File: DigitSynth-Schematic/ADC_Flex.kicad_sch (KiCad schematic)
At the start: 3 parts, among them U1 ADS1256IDBR

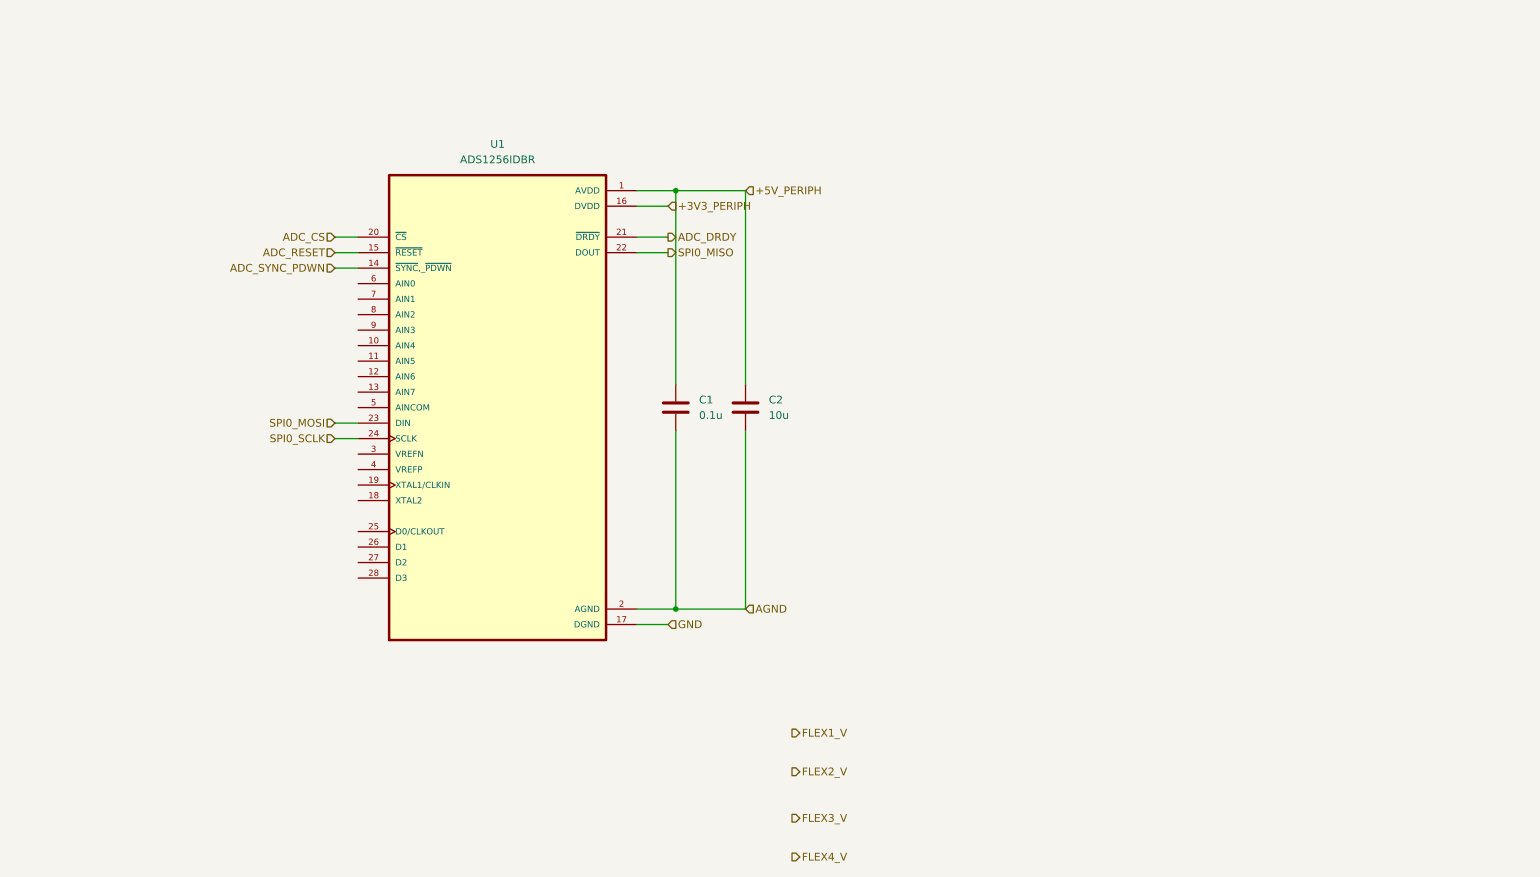
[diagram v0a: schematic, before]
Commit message: Add completed KiCad schematic hierarchy (Pi interface, ADC, LEDs, buttons, power)
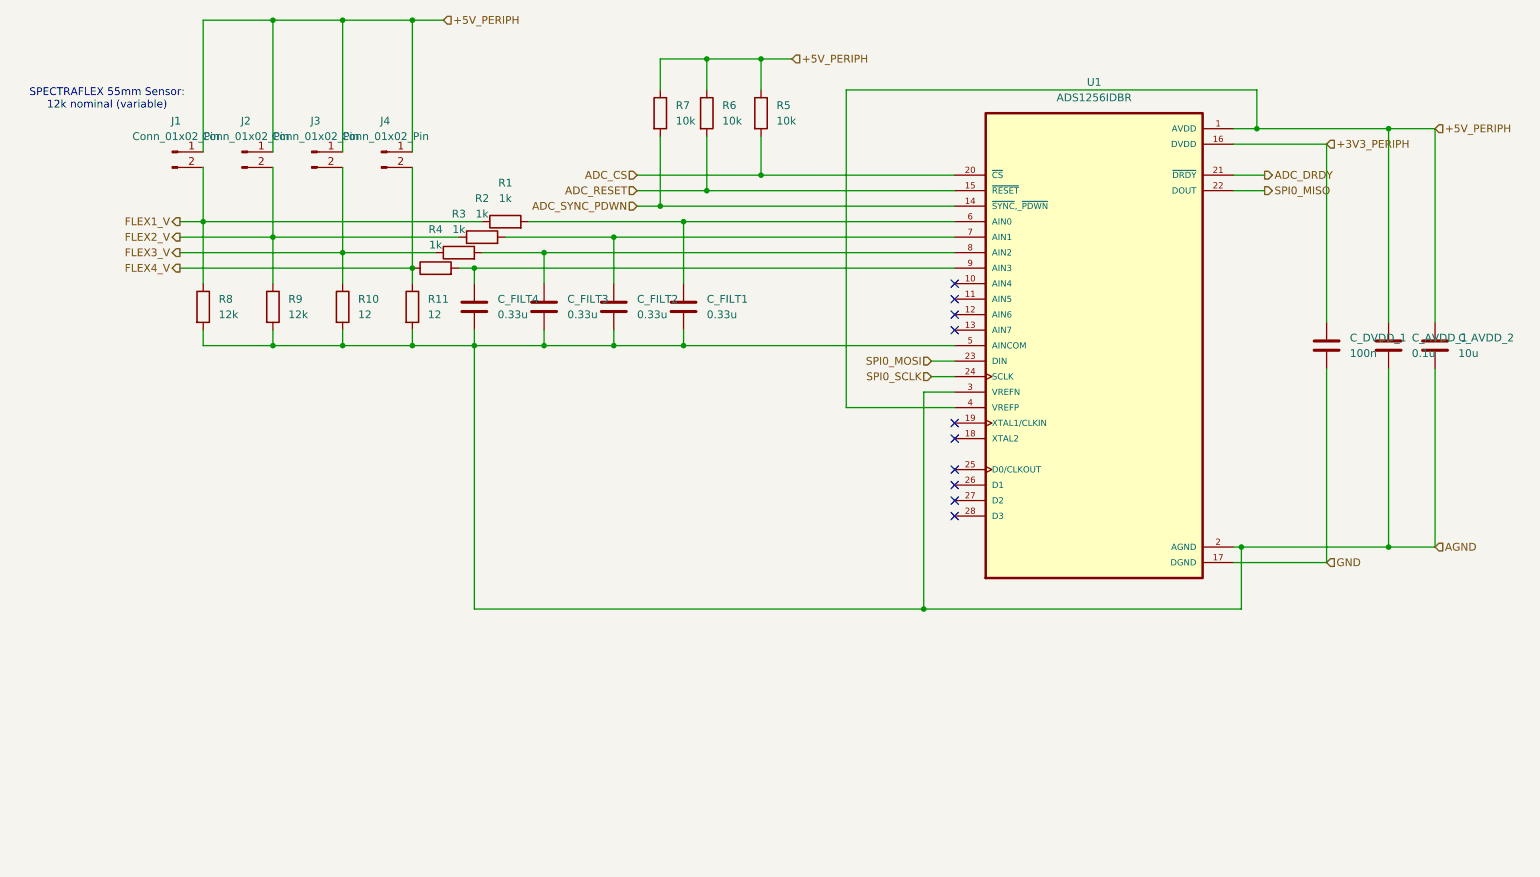
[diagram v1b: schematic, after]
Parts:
- added C_DVDD_1: 100n, symbol Device:C
- added C_FILT1, C_FILT2, C_FILT3, C_FILT4: 0.33u, symbol Device:C
- added J1, J2, J3, J4: Conn_01x02_Pin, symbol Connector:Conn_01x02_Pin
- added R1, R2, R3, R4: 1k, symbol Device:R
- added R10, R11: 12, symbol Device:R
- added R5, R6, R7: 10k, symbol Device:R
- added R8, R9: 12k, symbol Device:R
- renumbered C1 to C_AVDD_1, C2 to C_AVDD_2
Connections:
- net +3V3_PERIPH: now also C_DVDD_1.1
- net +5V_PERIPH: now also U1.4 (VREFP), J1.1 (Pin_1), J2.1 (Pin_1), J3.1 (Pin_1), J4.1 (Pin_1), R5.1, R6.1, R7.1
- net ADC_CS: now also R5.2
- net ADC_RESET: now also R6.2
- net ADC_SYNC_PDWN: now also R7.2
- net AGND: now also U1.3 (VREFN), U1.5 (AINCOM), C_FILT1.2, C_FILT2.2, C_FILT3.2, C_FILT4.2, R10.2, R11.2, R8.2, R9.2
- net FLEX1_V: now also J1.2 (Pin_2), R1.1, R8.1
- net FLEX2_V: now also J2.2 (Pin_2), R2.1, R9.1
- net FLEX3_V: now also J3.2 (Pin_2), R10.1, R3.1
- net FLEX4_V: now also J4.2 (Pin_2), R11.1, R4.1
- net GND: now also C_DVDD_1.2
- net at U1.6 (AIN0): now also C_FILT1.1, R1.2
- net at U1.7 (AIN1): now also C_FILT2.1, R2.2
- net at U1.8 (AIN2): now also C_FILT3.1, R3.2
- net at U1.9 (AIN3): now also C_FILT4.1, R4.2
- no-connect marks 0 -> 10
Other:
- note added: "SPECTRAFLEX 55mm Sensor: 12k nominal (variable)"
- moved on the sheet: C_AVDD_1, C_AVDD_2, U1
